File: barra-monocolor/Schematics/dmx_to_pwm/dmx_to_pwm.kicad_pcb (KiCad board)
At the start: 2 copper layers, 46 x 171.8 mm, 69 parts, among them J1 RJ45, J2 RJ45, J4 Conn_01x03_Socket, J5 Conn_02x06_Counter_Clockwise, J6 Conn_01x07_Socket, Q1 TIP41, Q2 TIP41, Q3 TIP41, Q4 TIP41, Q5 TIP41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

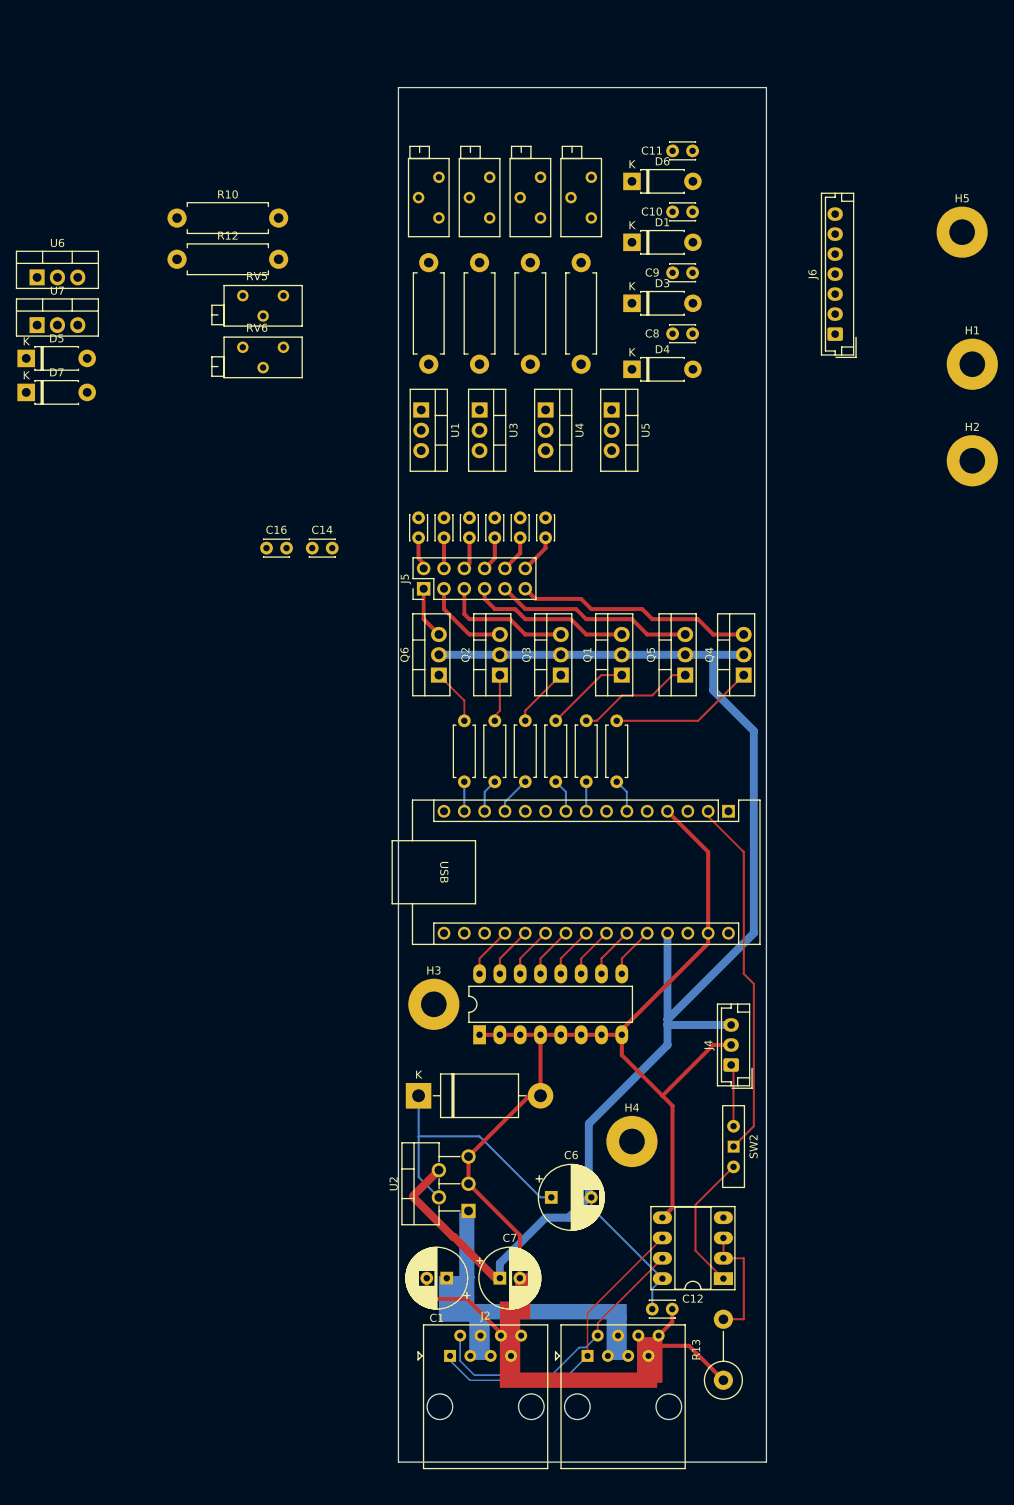
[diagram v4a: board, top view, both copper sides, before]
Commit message: updated pcb for 6 lasers
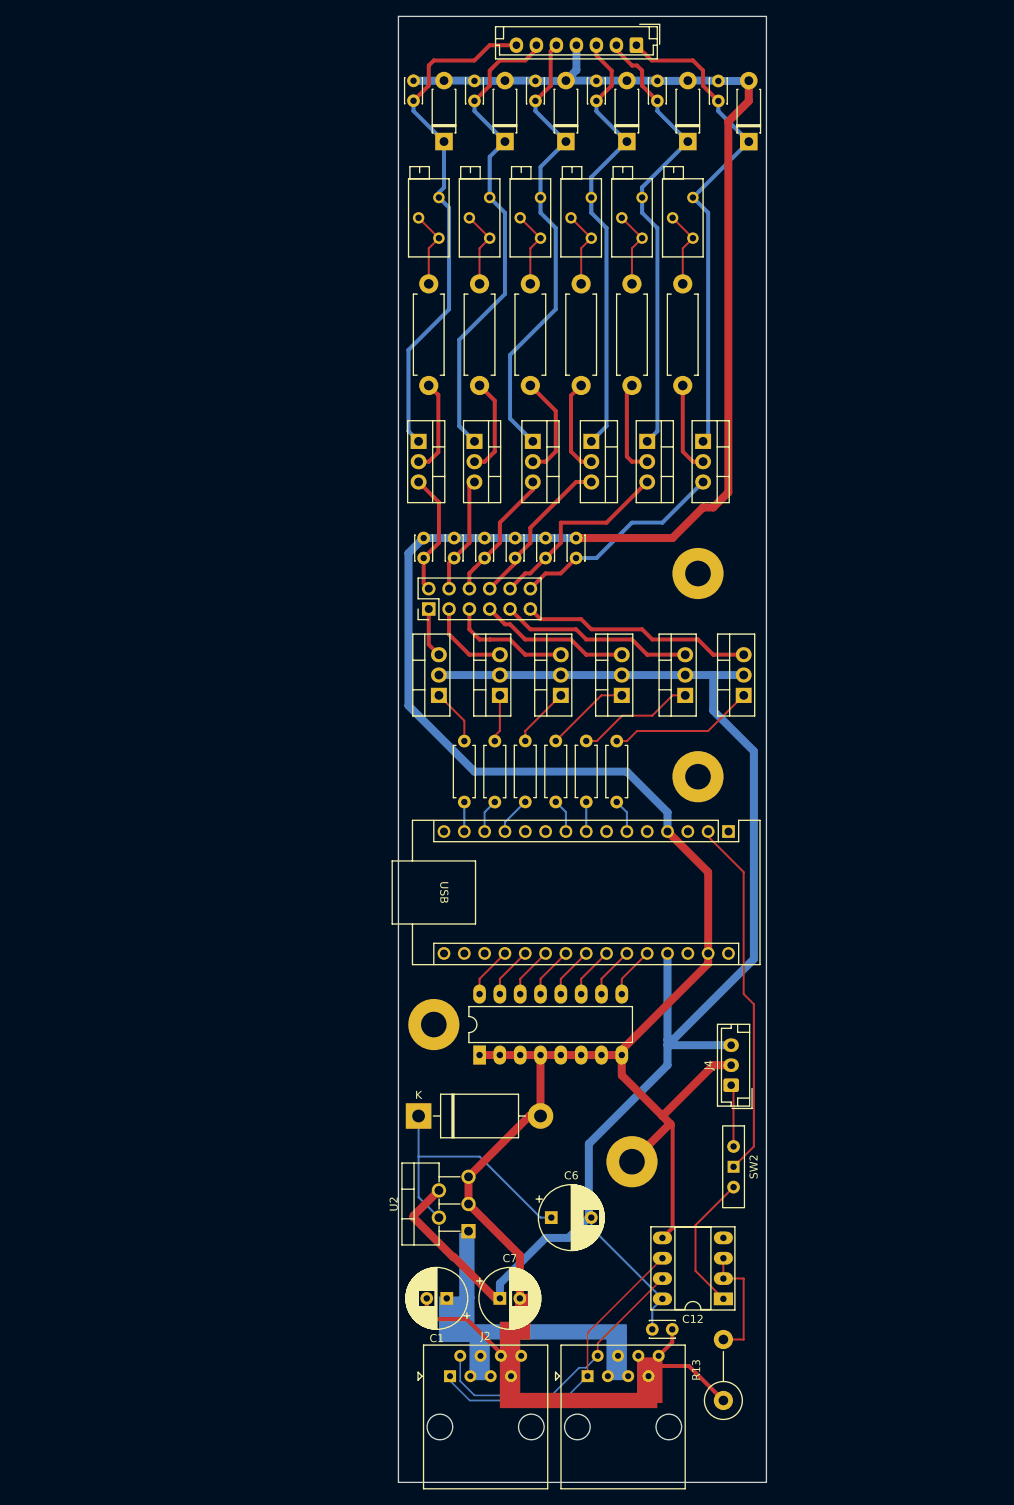
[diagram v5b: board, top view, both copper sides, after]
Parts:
- removed H5: MountingHole_Pad, MountingHole:MountingHole_3.2mm_M3_Pad
- moved D5 94.3 mm to (116.2, 29.2), turned to 90 degrees
- moved U6 85.7 mm to (110.5, 66.7), turned to -90 degrees
- moved C14 77.4 mm to (112.4, 21.6), turned to -90 degrees
- moved R10 63.7 mm to (108.0, 47.0), turned to -90 degrees
- moved H1 61.9 mm to (109.9, 108.6)
- moved C16 61.2 mm to (74.3, 21.6), turned to -90 degrees
- moved D7 60.9 mm to (78.1, 29.2), turned to 90 degrees
- moved RV5 51.7 mm to (109.2, 41.3), turned to -90 degrees
- moved U7 49.8 mm to (74.9, 66.7), turned to -90 degrees
- moved J6 43.8 mm to (102.2, 17.1), turned to 180 degrees
- moved H2 37.1 mm to (109.9, 83.2)
- moved C8 31.9 mm to (104.8, 21.6), turned to -90 degrees
- moved R12 31.6 mm to (76.2, 47.0), turned to -90 degrees
- moved D4 29.3 mm to (108.6, 29.2), turned to 90 degrees
- moved C11 28.6 mm to (81.9, 21.6), turned to -90 degrees
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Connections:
- H4 pad 1: unconnected-(H4-Pad1) -> GND
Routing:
- net GND: track 166.0 -> 374.9 mm
- net Net-(D7-K): track 0.00 -> 64.8 mm
- net Net-(D5-K): track 0.00 -> 62.3 mm
- net Net-(D6-K): track 0.00 -> 60.9 mm
- net Net-(D1-K): track 0.00 -> 57.8 mm
- net Net-(D4-K): track 0.00 -> 57.3 mm
- net Net-(D3-K): track 0.00 -> 56.1 mm
- net L1-SOC-OUT: track 4.88 -> 27.1 mm
- net L2-SOC-OUT: track 4.62 -> 24.2 mm
- net L3-SOC-OUT: track 4.36 -> 19.7 mm
- net Net-(U3-VO): track 0.00 -> 13.0 mm
- net L4-SOC-OUT: track 4.09 -> 16.6 mm
- net Net-(U1-VO): track 0.00 -> 12.1 mm
- net Net-(U5-VO): track 0.00 -> 12.0 mm
- net Net-(U4-VO): track 0.00 -> 11.8 mm
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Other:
- board size 46 x 171.8 mm -> 46 x 183.2 mm

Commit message: improved pcb
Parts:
- moved H2 3.70 mm to (113.0, 81.3)
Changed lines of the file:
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@@
 	(footprint "MountingHole:MountingHole_3.2mm_M3_Pad"
 		(layer "F.Cu")
-		(at 109.855 83.185)
+		(at 113.03 81.28)
 		(descr "Mounting Hole 3.2mm, M3")
 		(tags "mounting hole 3.2mm m3")
@@
 		)
 		(fp_text user "${REFERENCE}"
-			(at 1.27 6.35 360)
+			(at 1.27 6.35 0)
 			(layer "F.Fab")
 			(effects
@@
 		(tags "connector JST EH vertical")
 		(property "Reference" "J6"
-			(at 7.5 -2.8 360)
+			(at 7.5 -2.8 0)
 			(layer "F.SilkS")
 			(hide yes)
@@
 		)
 		(property "Value" "Conn_01x07_Socket"
-			(at 7.5 3.4 360)
+			(at 7.5 3.4 0)
 			(layer "F.Fab")
 			(hide yes)
@@
 		)
 		(fp_text user "${REFERENCE}"
-			(at 7.5 1.5 360)
+			(at 7.5 1.5 0)
 			(layer "F.Fab")
 			(effects
@@
 		(start 101.6 42.535)
 		(end 102.87 41.265)
-		(width 0.25)
+		(width 0.5)
 		(layer "F.Cu")
 		(net 39)
@@
 		(start 101.6 46.98)
 		(end 101.6 42.535)
-		(width 0.25)
+		(width 0.5)
 		(layer "F.Cu")
 		(net 39)
@@
 		(start 102.87 41.265)
 		(end 100.33 38.725)
-		(width 0.25)
+		(width 0.5)
 		(layer "F.Cu")
 		(net 39)
@@
 		(start 95.25 46.98)
 		(end 95.25 42.535)
-		(width 0.25)
+		(width 0.5)
 		(layer "F.Cu")
 		(net 43)
@@
 		(start 95.25 42.535)
 		(end 96.52 41.265)
-		(width 0.25)
+		(width 0.5)
 		(layer "F.Cu")
 		(net 43)
@@
 		(start 96.52 41.265)
 		(end 93.98 38.725)
-		(width 0.25)
+		(width 0.5)
 		(layer "F.Cu")
 		(net 43)
@@
 		(start 88.9 46.98)
 		(end 88.9 42.535)
-		(width 0.25)
+		(width 0.5)
 		(layer "F.Cu")
 		(net 44)
@@
 		(start 88.9 42.535)
 		(end 90.17 41.265)
-		(width 0.25)
+		(width 0.5)
 		(layer "F.Cu")
 		(net 44)
@@
 		(start 90.17 41.265)
 		(end 87.63 38.725)
-		(width 0.25)
+		(width 0.5)
 		(layer "F.Cu")
 		(net 44)
@@
 		(start 82.55 46.98)
 		(end 82.55 42.535)
-		(width 0.25)
+		(width 0.5)
 		(layer "F.Cu")
 		(net 45)
@@
 		(start 83.82 41.265)
 		(end 81.28 38.725)
-		(width 0.25)
+		(width 0.5)
 		(layer "F.Cu")
 		(net 45)
@@
 		(start 82.55 42.535)
 		(end 83.82 41.265)
-		(width 0.25)
+		(width 0.5)
 		(layer "F.Cu")
 		(net 45)
@@
 		(start 107.95 46.98)
 		(end 107.95 42.535)
-		(width 0.25)
+		(width 0.5)
 		(layer "F.Cu")
 		(net 74)
@@
 		(start 109.22 41.265)
 		(end 106.68 38.725)
-		(width 0.25)
+		(width 0.5)
 		(layer "F.Cu")
 		(net 74)
@@
 		(start 107.95 42.535)
 		(end 109.22 41.265)
-		(width 0.25)
+		(width 0.5)
 		(layer "F.Cu")
 		(net 74)
@@
 		(start 76.2 42.535)
 		(end 77.47 41.265)
-		(width 0.25)
+		(width 0.5)
 		(layer "F.Cu")
 		(net 76)
@@
 		(start 77.47 41.265)
 		(end 74.93 38.725)
-		(width 0.25)
+		(width 0.5)
 		(layer "F.Cu")
 		(net 76)
@@
 		(start 76.2 46.98)
 		(end 76.2 42.535)
-		(width 0.25)
+		(width 0.5)
 		(layer "F.Cu")
 		(net 76)
